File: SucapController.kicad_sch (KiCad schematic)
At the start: 44 parts, among them J1 Conn_01x14, J2 Conn_01x04, J3 Conn_01x02, J4 Conn_02x03_Counter_Clockwise, J5 Conn_02x03_Counter_Clockwise, J6 Conn_02x03_Counter_Clockwise, J7 Screw_Terminal_01x01, Q1 SI2301, U1 HX9193, U2 HX9193, U3 W25Q32JVSS, U4 STM32H750VBTx, U5 REF3030, U6 74LVC1G17, Y1 25M, Y2 32.768K

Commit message: Do some change
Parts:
- removed C1, C11, C13, C17, C2, C3, C4, C5, C6, C7, C8: 100n, Capacitor_SMD:C_0603_1608Metric, symbol Device:C_Small
- removed C12, C9: 10u, Capacitor_SMD:C_0603_1608Metric, symbol Device:C_Small
- removed C18, C19: 2.2u, Capacitor_SMD:C_0603_1608Metric, symbol Device:C_Small
- removed D1: LED, LED_SMD:LED_0603_1608Metric, symbol Device:LED
- removed J2: Conn_01x04, Connector_JST:JST_GH_SM04B-GHS-TB_1x04-1MP_P1.25mm_Horizontal, symbol Connector_Generic:Conn_01x04
- removed R1: 10K, Resistor_SMD:R_0603_1608Metric, symbol Device:R_Small
- removed R3: 1K, Resistor_SMD:R_0603_1608Metric, symbol Device:R_Small
- removed U1: HX9193, Package_TO_SOT_SMD:SOT-23-5_HandSoldering, symbol MyLib:HX9193
- removed U4: STM32H750VBTx, Package_QFP:LQFP-100_14x14mm_P0.5mm, symbol MCU_ST_STM32H7:STM32H750VBTx
- added C1, C11, C13, C19, C2, C3, C4, C5, C6, C7, C8: 100n, GENERAL_RCL_SMD:C0603(1608M), symbol Basic_passive_components:Capacitor
- added C12, C9: 10u, GENERAL_RCL_SMD:C0603(1608M), symbol Basic_passive_components:Capacitor
- added C17, C18: 2.2u, GENERAL_RCL_SMD:C0603(1608M), symbol Basic_passive_components:Capacitor
- added D1: LED, symbol Basic_semiconductor:Diode_LED
- added J2: (no value), symbol Link_W2B_connector:Conn_01x04
- added R1: 100n, GENERAL_RCL_SMD:R0603(1608M), symbol Basic_passive_components:Resistor
- added R3: 1k, GENERAL_RCL_SMD:R0603(1608M), symbol Basic_passive_components:Resistor
- added U1: HX9193-33GB, GENERAL_SMALL-SEMI_SMD:SOT-23-5, symbol Power_LDO:HX9193-33GB
- added U4: STM32H750VBT6, GENERAL_LARGE-SEMI_SMD:QFP-1414_100, symbol Integrated-circuit_micro-controller:STM32H750VBT6
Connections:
- net +3V0: now also C8.2, U4.6 (Vbat)
- net +3V3: now also C1.2, C12.2, C13.2, C2.2, C3.2, C4.2, C5.2, C6.2, C7.2, J2.1, R1.2, R3.2, U1.5 (VOUT), U4.100 (Vin), U4.11 (Vin), U4.21 (Vin_A), U4.27 (Vin), U4.50 (Vin), U4.75 (Vin)
- net +5V: now also C11.2, C9.2, U1.1 (VIN), U1.3 (EN)
- net ADC_I1: now also U4.30 (PA6)
- net ADC_I2: now also U4.31 (PA7)
- net ADC_V1: now also U4.32 (PC4)
- net ADC_V2: now also U4.33 (PC5)
- net ADC_V3: now also U4.34 (PB0)
- net CAP_Boost: now also U4.40 (PE10)
- net CENTER: now also U4.87 (PD6)
- net CHG_EN: now also U4.41 (PE11)
- net CHG_ISET: now also U4.28 (PA4)
- net DOWN: now also U4.86 (PD5)
- net EN_MOS: now also U4.39 (PE9)
- net GND: now also C1.1, C11.1, C12.1, C13.1, C17.2, C18.2, C19.1, C2.1, C3.1, C4.1, C5.1, C6.1, C7.1, C8.1, C9.1, D1.1 (Cathode), J2.4, U1.2 (GND), U4.10 (GND), U4.19 (GND_A), U4.26 (GND), U4.49 (GND), U4.74 (GND), U4.94 (BOOT0), U4.99 (GND)
- net LCD_CS: now also U4.83 (PD2)
- net LCD_DC: now also U4.82 (PD1)
- net LCD_EN: now also U4.78 (PC10)
- net LCD_RST: now also U4.81 (PD0)
- net LCD_SCL: now also U4.79 (PC11)
- net LCD_SDA: now also U4.80 (PC12)
- net LEFT: now also U4.85 (PD4)
- net OSC32_IN: now also U4.8 (PC14)
- net OSC32_OUT: now also U4.9 (PC15)
- net OSC_IN: now also U4.12 (PH0)
- net OSC_OUT: now also U4.13 (PH1)
- net RIGHT: now also U4.88 (PD7)
- net SPI1_CS: now also U4.92 (PB6)
- net SPI1_MISO: now also U4.90 (PB4)
- net SPI1_MOSI: now also U4.91 (PB5)
- net SPI1_SCK: now also U4.89 (PB3)
- net SWCLK: now also J2.3, U4.76 (PA14)
- net SWDIO: now also J2.2, U4.72 (PA13)
- net UART1_RX: now also U4.54 (PB15)
- net UART1_TX: now also U4.53 (PB14)
- net UART2_RX: now also U4.25 (PA3)
- net UART2_TX: now also U4.24 (PA2)
- net UP: now also U4.84 (PD3)
- net VREF: now also U4.20 (Vref+)
- new net: C19.2, R1.1, U4.14 (nRST)
- new net: C17.1, U4.48 (Vcap_1)
- new net: D1.2 (Anode), R3.1
- new net: C18.1, U4.73 (Vcap_2)

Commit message: do some change
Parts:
- removed C20: 100n, Capacitor_SMD:C_0603_1608Metric, symbol Device:C_Small
- added C20: 100n, GENERAL_RCL_SMD:C0603(1608M), symbol Basic_passive_components:Capacitor
- C10, C14, C15, C16, C21, C22: footprint Capacitor_SMD:C_0603_1608Metric -> GENERAL_RCL_SMD:C0603(1608M); symbol Device:C_Small -> Basic_passive_components:Capacitor
- C23, C24: symbol Device:C_Small -> Basic_passive_components:Capacitor
- D1: footprint (none) -> GENERAL_2-PIN_PLASTIC_SMD:LED0603(1608M)
- J1: symbol Connector_Generic:Conn_01x14 -> Link_W2B_connector:Conn_01x14
- J3: symbol Connector_Generic:Conn_01x02 -> Link_W2B_connector:Conn_01x02
- J4, J5, J6: symbol Connector_Generic:Conn_02x03_Counter_Clockwise -> Link_W2B_connector:Conn_02x03
- J7: symbol Connector:Screw_Terminal_01x01 -> Link_W2B_connector:Conn_01x01
- R2: footprint Resistor_SMD:R_0603_1608Metric -> GENERAL_RCL_SMD:R0603(1608M); symbol Device:R_Small -> Basic_passive_components:Resistor
- U2: footprint Package_TO_SOT_SMD:SOT-23-5_HandSoldering -> GENERAL_SMALL-SEMI_SMD:SOT-23-5; symbol MyLib:HX9193 -> Power_LDO:HX9193-33GB
- U3: footprint Package_SO:SOIC-8_5.23x5.23mm_P1.27mm -> GENERAL_MIDDLE-SEMI_SMD:SOIC-5252_8; symbol Memory_Flash:W25Q32JVSS -> Integrated-circuit_storage:W25Q32JVSS
- U5: symbol Reference_Voltage:REF3030 -> Integrated-circuit_sensor:REF3030
- U6: symbol 74xGxx:74LVC1G17 -> integrated-circuit_logic:74LVC1G17
- Y1: symbol Device:Crystal_GND24 -> Basic_crystal_and_oscillator:Xtal-4
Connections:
- net +3V3: no longer C1.2, C2.2, C3.2, C4.2, C5.2, C6.2, C7.2, J2.1, R1.2, U3.7 (IO3), U3.8 (VCC), U4.100 (Vin), U4.11 (Vin), U4.21 (Vin_A), U4.27 (Vin), U4.50 (Vin), U4.75 (Vin)
- net GND: now also C20.1
- net RNSET: now reaches C19.2, R1.1, U4.14 (nRST)
- new net VCC: C1.2, C2.2, C20.2, C3.2, C4.2, C5.2, C6.2, C7.2, J2.1, R1.2, U3.7 (~{HOLD}), U3.8 (VCC), U4.100 (Vin), U4.11 (Vin), U4.21 (Vin_A), U4.27 (Vin), U4.50 (Vin), U4.75 (Vin)
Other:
- note added: "改成TL431"
- moved on the sheet: Q1, R1, U3

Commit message: Turn the footprints into ours
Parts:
- removed J3: Conn_01x02, Connector_Hirose:Hirose_DF13-02P-1.25DSA_1x02_P1.25mm_Vertical, symbol Link_W2B_connector:Conn_01x02
- C23, C24: footprint Capacitor_SMD:C_0603_1608Metric -> GENERAL_RCL_SMD:C0603(1608M)
- J1: footprint Connector_FFC-FPC:Hirose_FH12-14S-0.5SH_1x14-1MP_P0.50mm_Horizontal -> MECHANICAL_EDGE-CONN:FFC_14
- J2: footprint (none) -> CONNECTOR_GH_SMD:GH1.25_H_4
- J4, J5, J6: footprint Connector_PinHeader_1.27mm:PinHeader_2x03_P1.27mm_Vertical_SMD -> CONNECTOR_PINHEADER_SMD:PINHEADER_02x03_1.27mm
- Q1: footprint Package_TO_SOT_SMD:SOT-23 -> GENERAL_SMALL-SEMI_SMD:SOT-23; symbol Device:Q_PMOS_GSD -> Basic_semiconductor:MOSFET_P-ch
- U5: footprint Package_TO_SOT_SMD:SOT-23 -> GENERAL_SMALL-SEMI_SMD:SOT-23
- U6: footprint Package_TO_SOT_SMD:SOT-353_SC-70-5 -> GENERAL_SMALL-SEMI_SMD:SOT-353
- Y1: footprint Crystal:Crystal_SMD_3225-4Pin_3.2x2.5mm -> GENERAL_XTAL_OSC_SMD:SMD-3225_4
- Y2: footprint Crystal:Crystal_SMD_3215-2Pin_3.2x1.5mm -> GENERAL_XTAL_OSC_SMD:SMD-3215_2; symbol Device:Crystal -> Basic_crystal_and_oscillator:Xtal-2
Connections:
- net +3V0 is gone; now on net +3V3: C8.2, U4.6 (Vbat)
- net RNSET is gone; now on net RESET: C19.2, R1.1, U4.14 (nRST)
- net VCC is gone; now on net +3V3: C1.2, C2.2, C20.2, C3.2, C4.2, C5.2, C6.2, C7.2, J2.1, R1.2, U3.7 (~{HOLD}), U3.8 (VCC), U4.100 (Vin), U4.11 (Vin), U4.21 (Vin_A), U4.27 (Vin), U4.50 (Vin), U4.75 (Vin)
- net OSC32_IN: now also Y2.2; no longer Y2.1
- net OSC32_OUT: now also Y2.1; no longer Y2.2
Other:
- moved on the sheet: C23

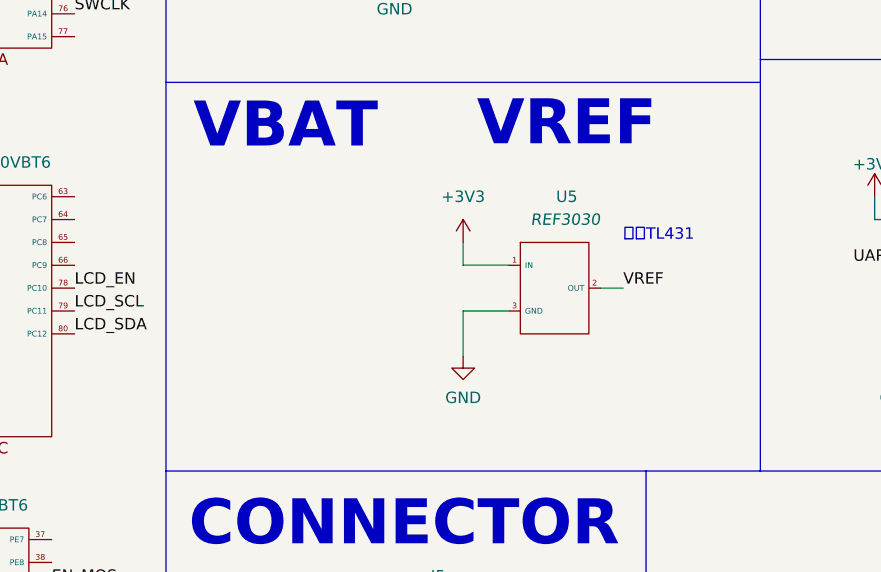
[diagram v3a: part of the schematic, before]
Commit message: Turn REF3030 into TL431
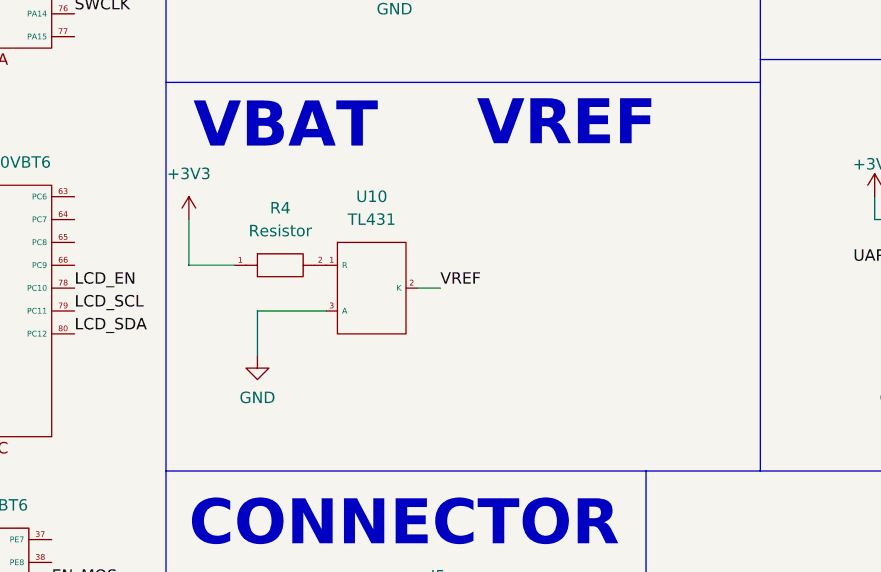
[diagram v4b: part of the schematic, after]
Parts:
- removed U5: REF3030, GENERAL_SMALL-SEMI_SMD:SOT-23, symbol Integrated-circuit_sensor:REF3030
- added R4: Resistor, GENERAL_RCL_SMD:R0603(1608M), symbol Basic_passive_components:Resistor
- added U10: TL431, GENERAL_SMALL-SEMI_SMD:SOT-23, symbol Integrated-circuit_sensor:TL431
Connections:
- net +3V3: now also R4.1
- net GND: now also U10.3 (A)
- net VREF: now also U10.2 (K)
- new net: R4.2, U10.1 (R)
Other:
- note removed: "改成TL431"

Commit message: fix some error
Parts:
- J7: footprint MyLib:TestPoint -> GENERAL_HOLE:HOLE-04-03_1
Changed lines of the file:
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@@
       (effects (font (size 1.27 1.27)) (justify left) hide)
     )
-    (property "Footprint" "MyLib:TestPoint" (id 2) (at 256.54 109.22 0)
+    (property "Footprint" "GENERAL_HOLE:HOLE-04-03_1" (id 2) (at 256.54 109.22 0)
       (effects (font (size 1.27 1.27)) hide)
     )
@@
     )
     (path "/2e08f475-ee42-4a20-b1f8-60a249905852"
-      (reference "J7") (unit 1) (value "Screw_Terminal_01x01") (footprint "MyLib:TestPoint")
+      (reference "J7") (unit 1) (value "Screw_Terminal_01x01") (footprint "GENERAL_HOLE:HOLE-04-03_1")
     )
     (path "/a96d2ea9-a484-4ab3-ada3-7553f2399c09"

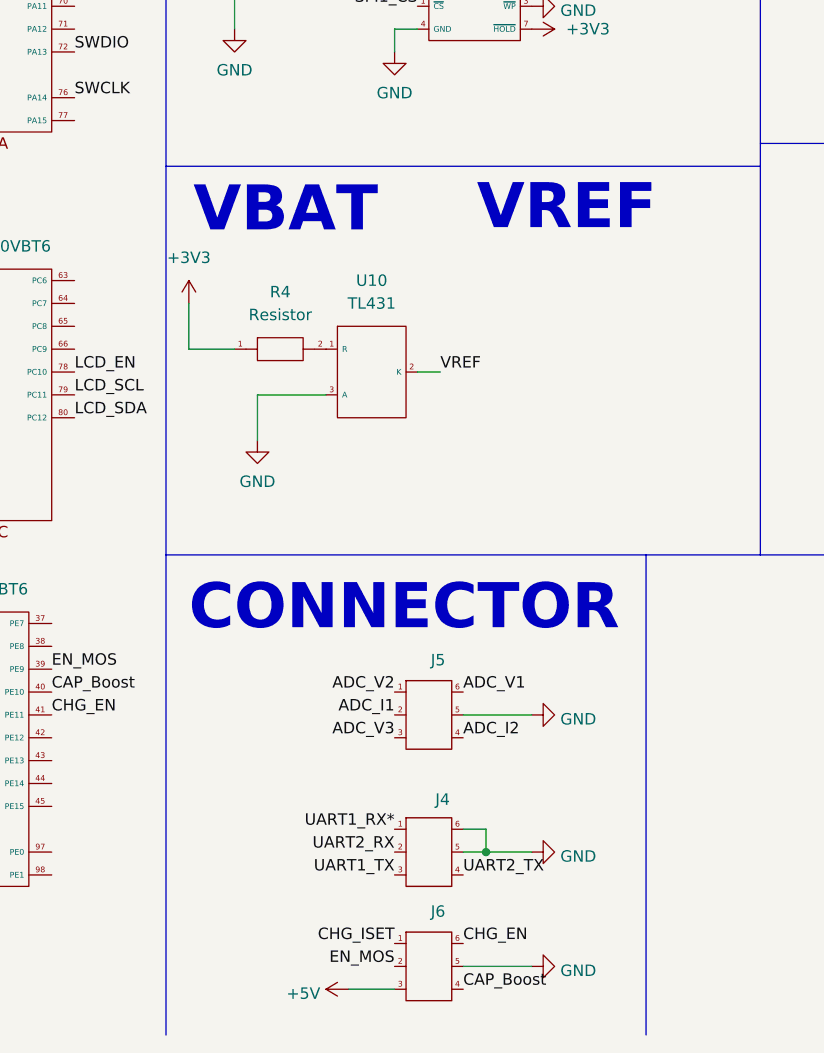
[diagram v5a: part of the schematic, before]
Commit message: fix some error of TL431
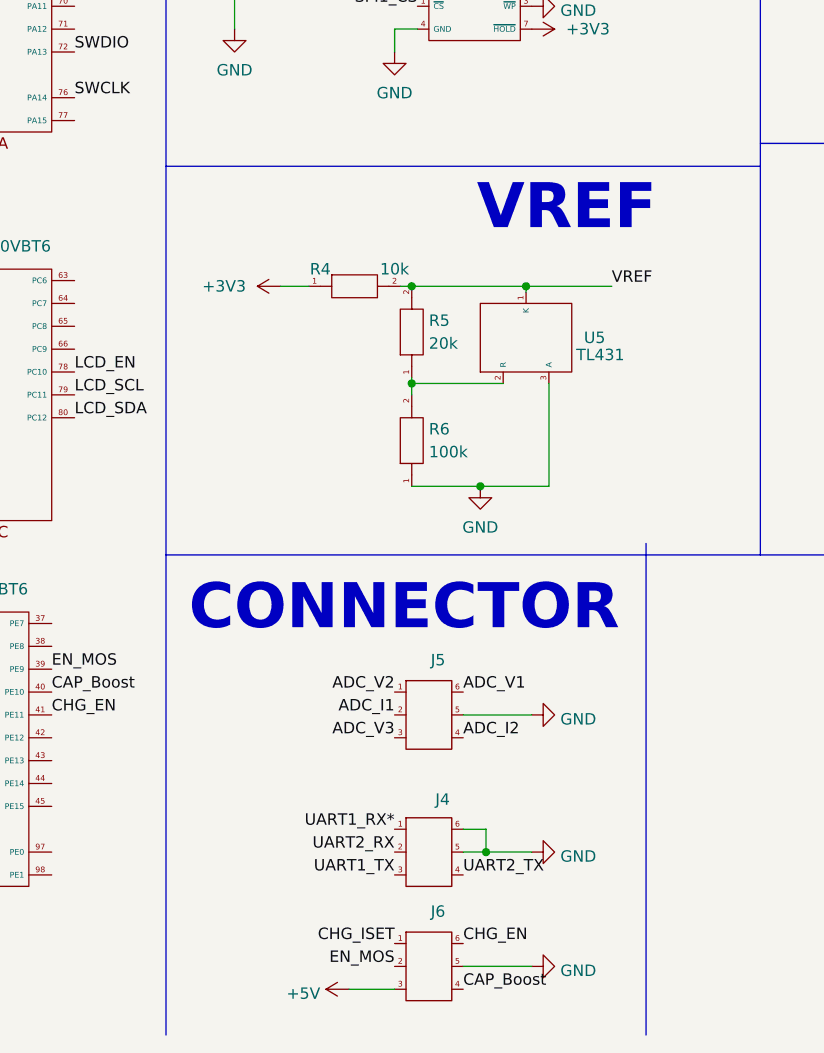
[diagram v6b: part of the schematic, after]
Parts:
- added R5: 20k, GENERAL_RCL_SMD:R0603(1608M), symbol Basic_passive_components:Resistor
- added R6: 100k, GENERAL_RCL_SMD:R0603(1608M), symbol Basic_passive_components:Resistor
- J7: footprint GENERAL_HOLE:HOLE-04-03_1 -> MECHANICAL:HOLE-04-03_1
- R4: value Resistor -> 10k
- U5: renamed from U10; symbol Integrated-circuit_sensor:TL431 -> Integrated-circuit_reference:TL431
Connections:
- net GND: now also R6.1
- net VREF: now also R4.2, U5.1 (K), R5.2; no longer U5.2 (K)
- new net: R5.1, R6.2, U5.2 (R)
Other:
- note removed: "VBAT"
- moved on the sheet: R4, U5
